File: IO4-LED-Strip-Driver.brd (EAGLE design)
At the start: 106 x 100 mm, 19 parts, among them Q1 DMN4468, Q2 DMN4468, Q3 DMN4468, Q7 DMN4468

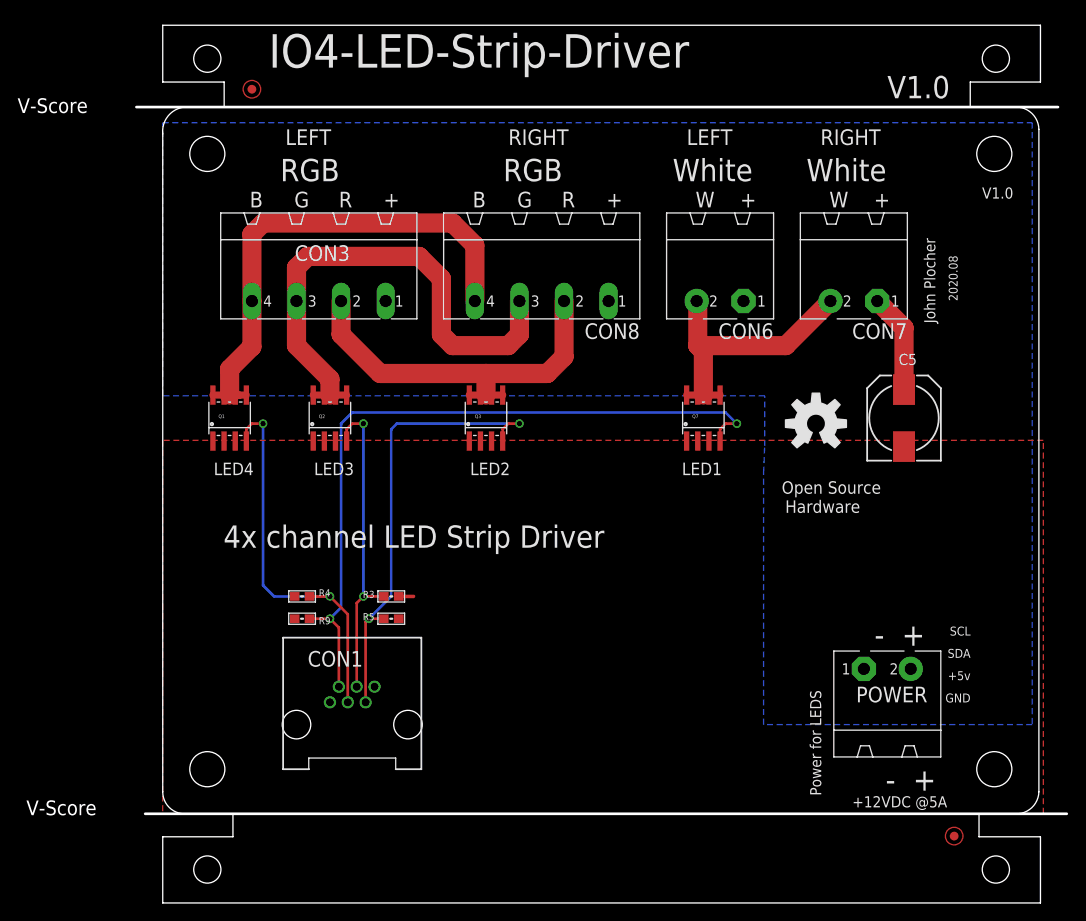
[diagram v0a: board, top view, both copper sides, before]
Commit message: FID placement & rerouting
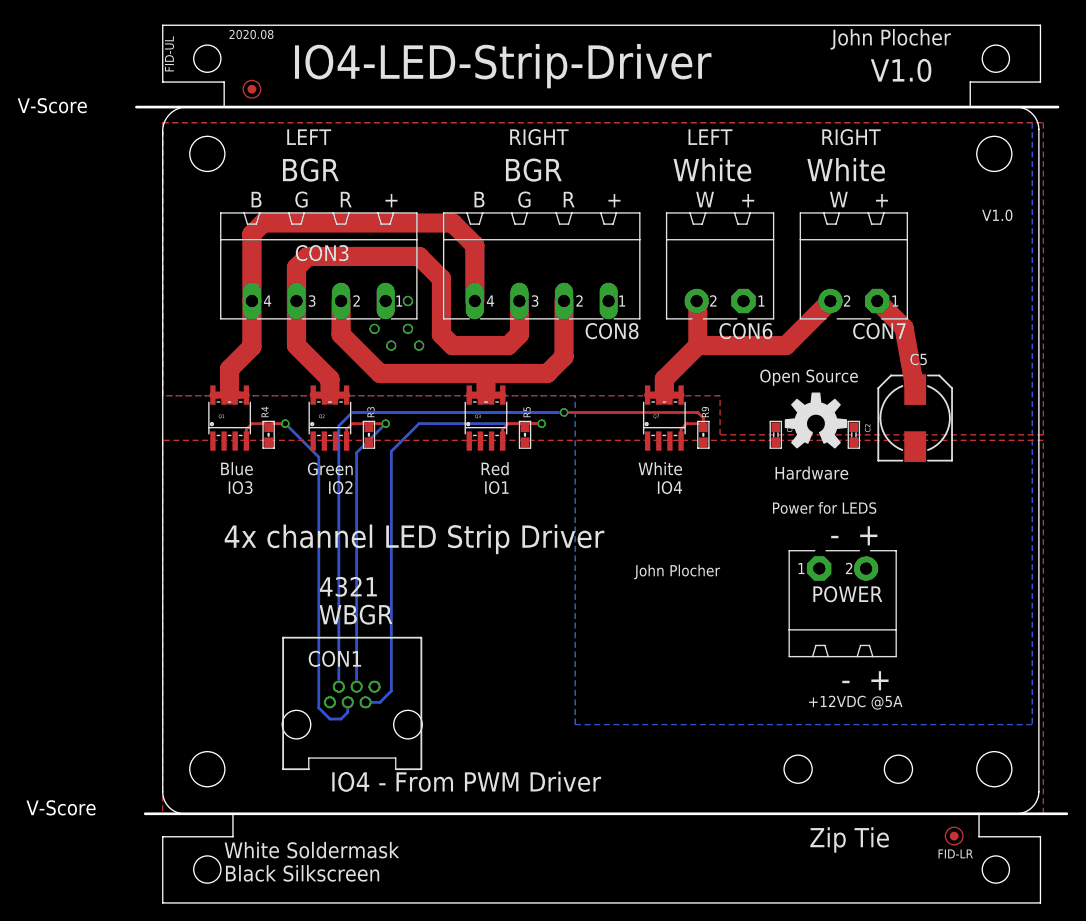
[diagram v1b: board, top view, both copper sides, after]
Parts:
- added C1: 10uF, SPCoast:0603-CAP
- added C2: 0.1uF, SPCoast:0603-CAP
- moved R9 50.3 mm to (61.6, 53.3), turned to 90 degrees
- moved R5 25.9 mm to (41.3, 53.3), turned to 90 degrees
- moved R4 18.8 mm to (12.1, 53.3), turned to 90 degrees
- moved R3 18.6 mm to (23.5, 53.3), turned to 90 degrees
- moved POWER 12.5 mm to (77.5, 33.0)
- moved Q7 4.45 mm to (57.1, 55.2)
- moved C5 1.27 mm to (85.7, 55.2)
- renumbered FID1 to FID-UL, FID2 to FID-LR
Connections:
- net +12V: now also C1.1, C2.1
- net GND: now also C1.2, C2.2
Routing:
- net WLED: track 82.9 -> 77.3 mm, vias 2 -> 1
- net RLED: track 52.4 -> 55.9 mm, vias 2 -> 1
- net GLED: track 36.1 -> 38.4 mm, vias 2 -> 1
- net GND: track 1.69 -> 0.00 mm
- net W: track 32.1 -> 33.4 mm
- net BLED: track 45.3 -> 45.7 mm, vias 2 -> 1
- net +12V: track 11.3 -> 11.5 mm, vias 0 -> 5
- added copper zone on layer 1, net +12V
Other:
- board text added: "4321"
- board text added: "4x channels: BGR + White Two connectors for driving Left and Right strings Each string can be up to 2.5m"
- board text added: "BGR"
- board text added: "Blue IO3"
- board text added: "Green IO2"
- board text added: "IO4 - From PWM Driver"
- board text added: "Red IO1"
- board text added: "WBGR"
- board text added: "White IO4"
- board text added: "White Soldermask Black Silkscreen"
- board text added: "Zip Tie"
- board text removed: "+5v"
- board text removed: "4x channels: RGB + White Two connectors for driving Left and Right strings Each string can be up to 2.5m"
- board text removed: "GND"
- board text removed: "LED1"
- board text removed: "LED2"
- board text removed: "LED3"
- board text removed: "LED4"
- board text removed: "RGB"
- board text removed: "SCL"
- board text removed: "SDA"

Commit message: Swapped R and G connector locations to match LED string wiring
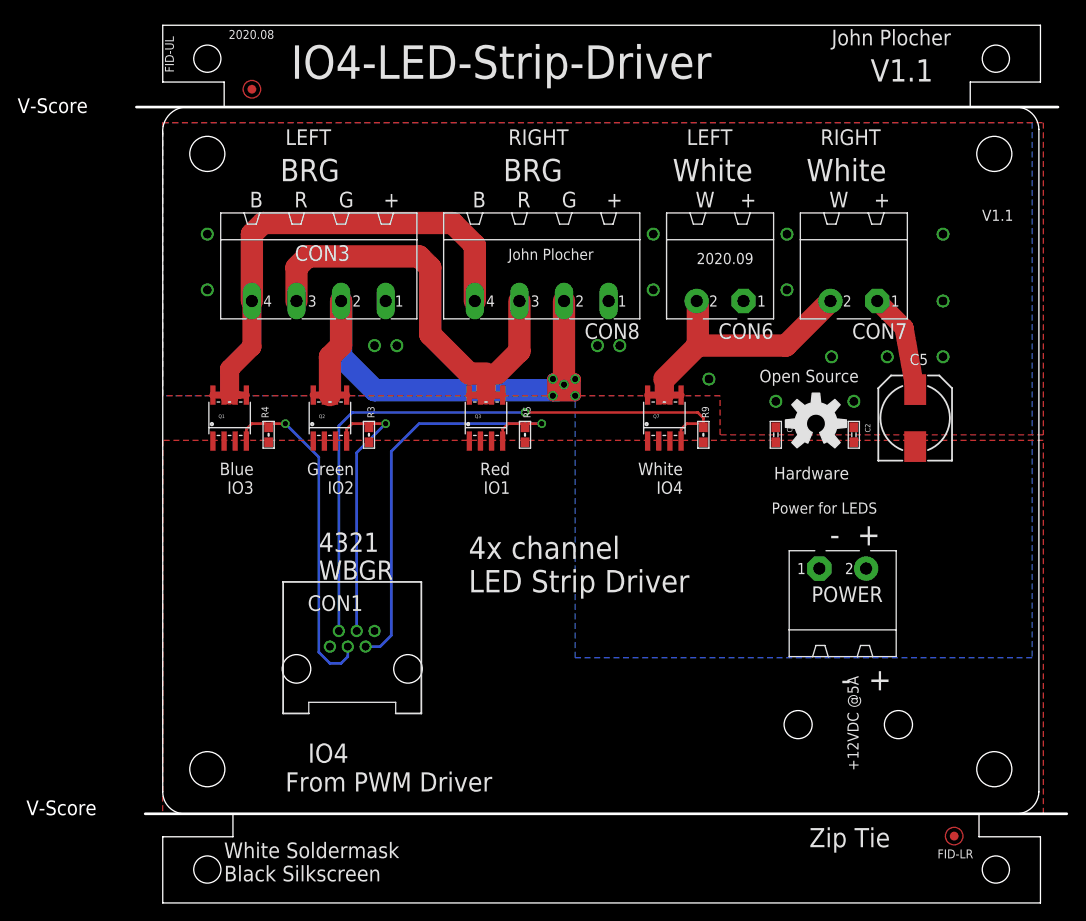
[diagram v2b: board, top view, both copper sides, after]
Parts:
- moved CON1 6.35 mm to (21.6, 26.7)
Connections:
- net G: now also CON3.2, CON8.2; no longer CON3.3, CON8.3
- net R: now also CON3.3, CON8.3; no longer CON3.2, CON8.2
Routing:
- net G: track 58.1 -> 79.0 mm, vias 0 -> 5
- net R: track 44.5 -> 52.8 mm
- net GLED: track 38.4 -> 32.1 mm
- net WLED: track 77.3 -> 71.0 mm
- net RLED: track 55.9 -> 49.5 mm
- net BLED: track 45.7 -> 39.3 mm
- net +12V: vias 5 -> 18
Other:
- board text added: "2020.09"
- board text added: "4x channels: GRB + White Two connectors for driving Left and Right strings Each string can be up to 2.5m long"
- board text added: "BRG"
- board text added: "IO4 From PWM Driver"
- board text added: "V1.1"
- board text removed: "4x channels: BGR + White Two connectors for driving Left and Right strings Each string can be up to 2.5m"
- board text removed: "BGR"
- board text removed: "IO4 - From PWM Driver"
- board text removed: "V1.0"

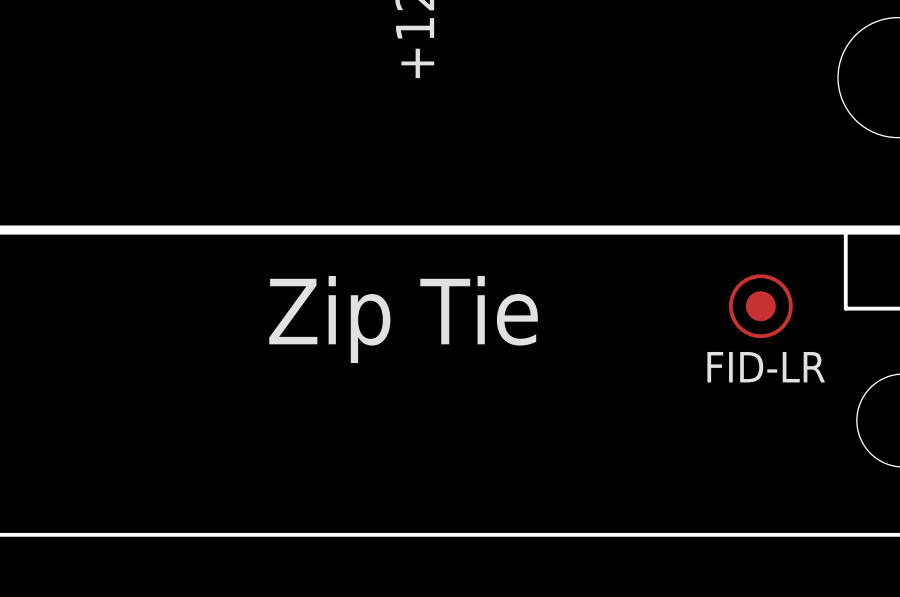
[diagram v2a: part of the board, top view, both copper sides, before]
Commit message: added values for connectors
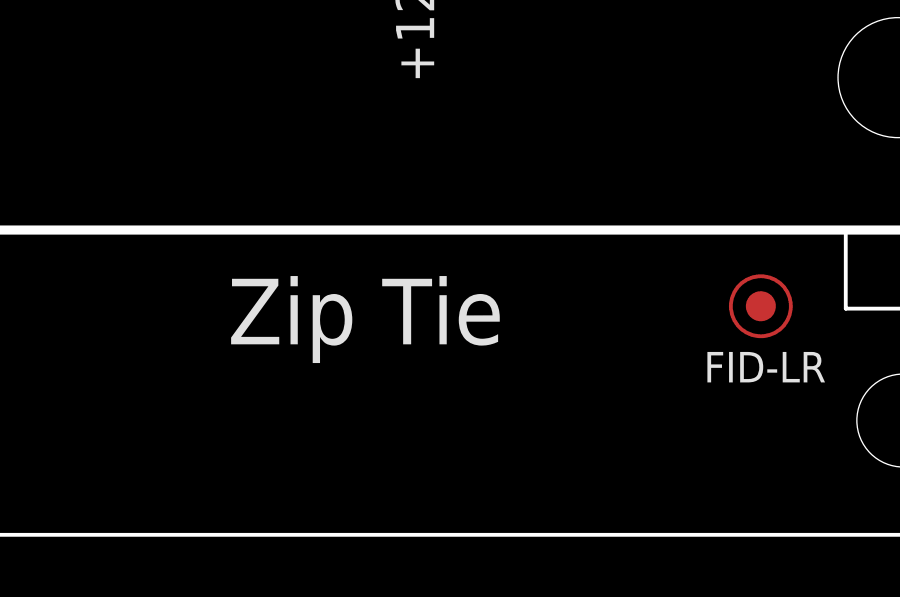
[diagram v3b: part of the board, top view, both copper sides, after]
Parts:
- CON1: value (none) -> RJ12/6
- CON3, CON6, CON7, CON8: value (none) -> 0.156
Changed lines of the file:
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@@
 <hole x="83.82" y="20.32" drill="3.2"/>
 <hole x="72.39" y="20.32" drill="3.2"/>
-<text x="73.66" y="6.35" size="2.1844" layer="21" font="vector" ratio="10">Zip Tie</text>
+<text x="72.39" y="6.35" size="2.1844" layer="21" font="vector" ratio="10">Zip Tie</text>
 <text x="67.31" y="74.055" size="1.27" layer="21" font="vector" ratio="10" rot="R180">2020.09</text>
 </plain>
@@
 <attribute name="NAME" x="55.88" y="55.245" size="0.4064" layer="25"/>
 </element>
-<element name="CON3" library="SPCoast" package="MSTBA4" value="" x="17.78" y="73.66" smashed="yes" rot="R180">
+<element name="CON3" library="SPCoast" package="MSTBA4" value="0.156" x="17.78" y="73.66" smashed="yes" rot="R180">
 <attribute name="NAME" x="21.336" y="74.93" size="1.778" layer="25" ratio="10" rot="R180"/>
 <attribute name="VALUE" x="27.94" y="73.66" size="1.778" layer="27" ratio="10" rot="R180"/>
@@
 <attribute name="VALUE" x="62.23" y="50.8" size="0.8128" layer="27" font="vector" rot="R180"/>
 </element>
-<element name="CON1" library="SPCoast" package="RJ25-INVERTED" value="" x="21.59" y="26.67"/>
-<element name="CON6" library="SPCoast" package="MSTBA2" value="" x="63.5" y="73.66" rot="R180"/>
-<element name="CON7" library="SPCoast" package="MSTBA2" value="" x="78.74" y="73.66" rot="R180"/>
-<element name="CON8" library="SPCoast" package="MSTBA4" value="" x="43.18" y="73.66" rot="R180"/>
+<element name="CON1" library="SPCoast" package="RJ25-INVERTED" value="RJ12/6" x="21.59" y="26.67"/>
+<element name="CON6" library="SPCoast" package="MSTBA2" value="0.156" x="63.5" y="73.66" rot="R180"/>
+<element name="CON7" library="SPCoast" package="MSTBA2" value="0.156" x="78.74" y="73.66" rot="R180"/>
+<element name="CON8" library="SPCoast" package="MSTBA4" value="0.156" x="43.18" y="73.66" rot="R180"/>
 <element name="FID-UL" library="SPCoast" package="FIDUCIAL_1MM" value="FIDUCIAL" x="10.16" y="92.71" smashed="yes">
 <attribute name="NAME" x="1.27" y="94.615" size="1.016" layer="25" rot="R90"/>

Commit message: added values for connectors
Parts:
- POWER: value (none) -> 0.156
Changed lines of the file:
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@@
 <attribute name="VALUE" x="27.94" y="73.66" size="1.778" layer="27" ratio="10" rot="R180"/>
 </element>
-<element name="POWER" library="SPCoast" package="MSTBA2" value="" x="77.47" y="33.02" smashed="yes">
+<element name="POWER" library="SPCoast" package="MSTBA2" value="0.156" x="77.47" y="33.02" smashed="yes">
 <attribute name="NAME" x="73.914" y="34.29" size="1.778" layer="25" ratio="10"/>
 <attribute name="VALUE" x="72.39" y="33.02" size="1.778" layer="27" ratio="10"/>

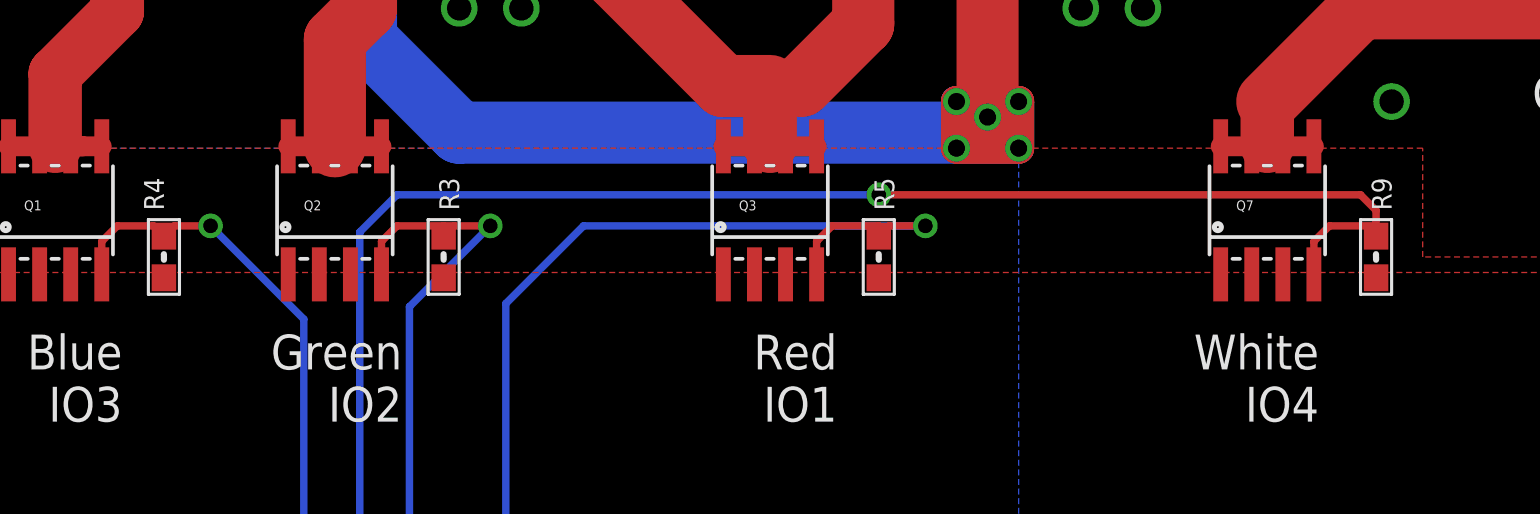
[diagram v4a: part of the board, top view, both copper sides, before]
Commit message: normalized values
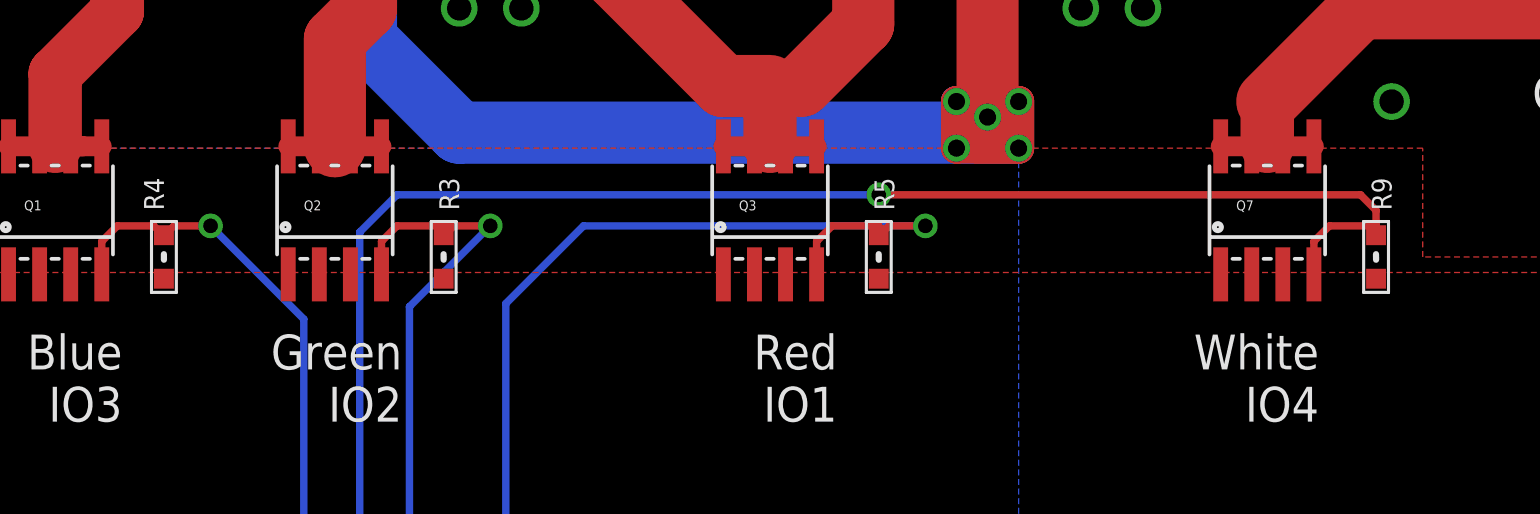
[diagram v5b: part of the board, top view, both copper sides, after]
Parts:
- BOARD1: value BOARD80X100 -> BOARD
- C2: value 0.1uF -> OSHW
- OSHW1: value OSHW-LOGOL -> OSHW
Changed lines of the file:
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@@
 </autorouter>
 <elements>
-<element name="BOARD1" library="SPCoast" package="BOARD-DINRAIL-3.17INX10CM" value="BOARD80X100" x="0" y="0"/>
-<element name="OSHW1" library="SparkFun" package="OSHW-LOGO-L" value="OSHW-LOGOL" x="74.422" y="54.61"/>
+<element name="BOARD1" library="SPCoast" package="BOARD-DINRAIL-3.17INX10CM" value="BOARD" x="0" y="0"/>
+<element name="OSHW1" library="SparkFun" package="OSHW-LOGO-L" value="OSHW" x="74.422" y="54.61"/>
 <element name="C5" library="SPCoast" package="0810-CAP" value="220uF" x="85.725" y="55.245" smashed="yes" rot="R90">
 <attribute name="NAME" x="87.195" y="62.565" size="1.27" layer="25" rot="R180"/>
@@
 </element>
 <element name="C1" library="SPCoast" package="0603-CAP" value="10uF" x="69.85" y="53.34" rot="R270"/>
-<element name="C2" library="SPCoast" package="0603-CAP" value="0.1uF" x="78.74" y="53.34" rot="R270"/>
+<element name="C2" library="SPCoast" package="0603-CAP" value="OSHW" x="78.74" y="53.34" rot="R270"/>
 </elements>
 <signals>
@@
 <wire x1="9.525" y1="53.975" x2="10.16" y2="54.61" width="0.3048" layer="1"/>
 <wire x1="10.16" y1="54.61" x2="11.645" y2="54.61" width="0.3048" layer="1"/>
-<wire x1="11.645" y1="54.61" x2="12.065" y2="54.19" width="0.3048" layer="1"/>
+<wire x1="11.645" y1="54.61" x2="12.065" y2="54.229" width="0.3048" layer="1"/>
 <via x="13.97" y="54.61" extent="1-16" drill="0.6"/>
 <wire x1="13.97" y1="54.61" x2="12.485" y2="54.61" width="0.3048" layer="1"/>
-<wire x1="12.485" y1="54.61" x2="12.065" y2="54.19" width="0.3048" layer="1"/>
+<wire x1="12.485" y1="54.61" x2="12.065" y2="54.229" width="0.3048" layer="1"/>
 <wire x1="21.082" y1="29.21" x2="21.082" y2="28.067" width="0.3048" layer="16"/>
 <wire x1="21.082" y1="28.067" x2="20.32" y2="27.305" width="0.3048" layer="16"/>
@@
 <wire x1="20.955" y1="53.975" x2="21.59" y2="54.61" width="0.3048" layer="1"/>
 <wire x1="21.59" y1="54.61" x2="23.495" y2="54.61" width="0.3048" layer="1"/>
-<wire x1="23.495" y1="54.61" x2="23.495" y2="54.19" width="0.3048" layer="1"/>
+<wire x1="23.495" y1="54.61" x2="23.495" y2="54.229" width="0.3048" layer="1"/>
 <wire x1="22.098" y1="30.988" x2="22.098" y2="51.308" width="0.3048" layer="16"/>
 <wire x1="22.098" y1="51.308" x2="25.4" y2="54.61" width="0.3048" layer="16"/>
 <via x="25.4" y="54.61" extent="1-16" drill="0.6"/>
 <wire x1="25.4" y1="54.61" x2="23.495" y2="54.61" width="0.3048" layer="1"/>
-<wire x1="23.915" y1="54.61" x2="23.495" y2="54.19" width="0.3048" layer="1"/>
+<wire x1="23.915" y1="54.61" x2="23.495" y2="54.229" width="0.3048" layer="1"/>
 </signal>
 <signal name="RLED">
@@
 <wire x1="38.735" y1="53.975" x2="39.37" y2="54.61" width="0.3048" layer="1"/>
 <wire x1="39.37" y1="54.61" x2="41.275" y2="54.61" width="0.3048" layer="1"/>
-<wire x1="41.275" y1="54.61" x2="41.275" y2="54.19" width="0.3048" layer="1"/>
+<wire x1="41.275" y1="54.61" x2="41.275" y2="54.229" width="0.3048" layer="1"/>
 <wire x1="29.21" y1="54.61" x2="43.18" y2="54.61" width="0.3048" layer="16"/>
 <via x="43.18" y="54.61" extent="1-16" drill="0.6"/>
 <wire x1="43.18" y1="54.61" x2="41.695" y2="54.61" width="0.3048" layer="1"/>
-<wire x1="41.695" y1="54.61" x2="41.275" y2="54.19" width="0.3048" layer="1"/>
+<wire x1="41.695" y1="54.61" x2="41.275" y2="54.229" width="0.3048" layer="1"/>
 <wire x1="29.21" y1="54.61" x2="26.035" y2="51.435" width="0.3048" layer="16"/>
 <wire x1="26.035" y1="51.435" x2="26.035" y2="30.48" width="0.3048" layer="16"/>
@@
 <wire x1="60.96" y1="55.88" x2="61.595" y2="55.245" width="0.3048" layer="1"/>
 <wire x1="61.595" y1="55.245" x2="61.595" y2="54.61" width="0.3048" layer="1"/>
-<wire x1="61.595" y1="54.61" x2="61.595" y2="54.19" width="0.3048" layer="1"/>
+<wire x1="61.595" y1="54.61" x2="61.595" y2="54.229" width="0.3048" layer="1"/>
 </signal>
 </signals>
